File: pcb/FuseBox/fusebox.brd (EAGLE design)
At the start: 160 x 100 mm, 102 parts, among them Q1 IRF510PbF, U1 ESP32-DEVKITC-32D, U2 TEXAS_INSTRUMENTS_TPS563249DD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, U3 MAXIM_ELECTRONICS_MAX7221CWGM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, U4 TEXAS_INSTRUMENTS_ADS1015IDGS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, U5 TEXAS_INSTRUMENTS_PCF8574PWTE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, U6 TEXAS_INSTRUMENTS_PCF8574PWTE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

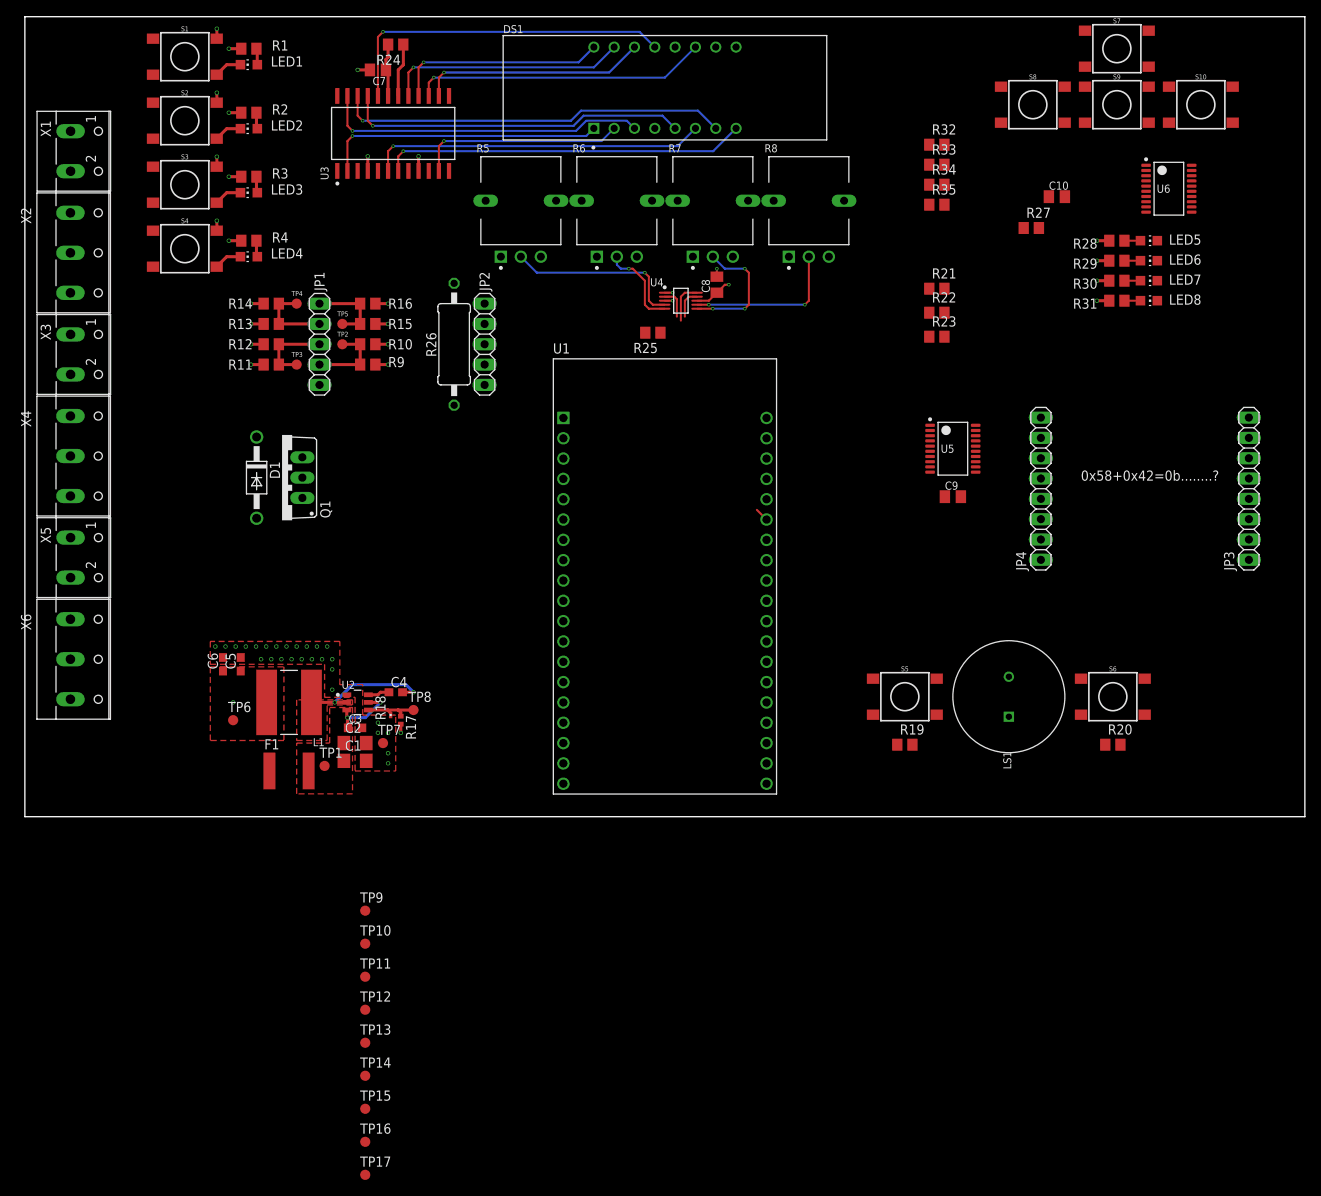
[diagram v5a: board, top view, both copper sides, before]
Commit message: Further work on PCB, almost done. Just have to route I2C and SPI lanes.
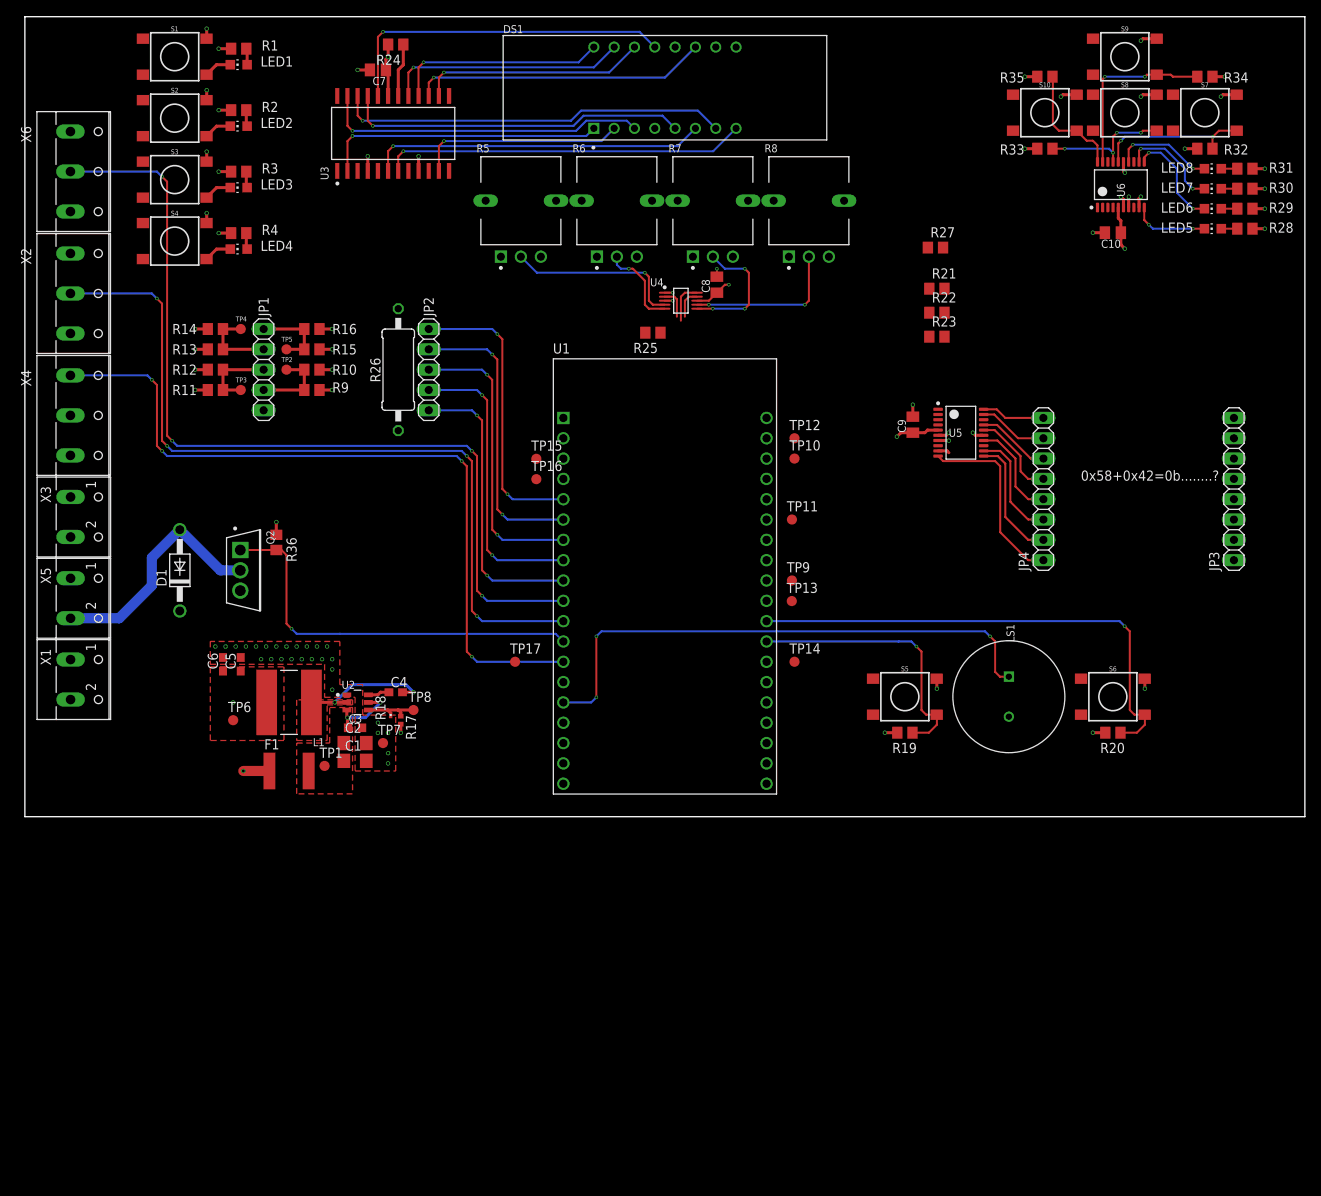
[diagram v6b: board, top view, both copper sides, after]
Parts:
- removed Q1: IRF510PbF, transistor-power:TO220BV
- added Q2: INFINEON_IRLB8721PBFINFINEON_IRLB8721PBF_0_0, Infineon - IRLB8721PbF:INFINEON_IRLB8721PBF_0
- added R36: 10k, rcl:R0805
- moved TP12 89.3 mm to (96.2, 47.3)
- moved TP16 85.6 mm to (63.9, 42.2)
- moved TP15 84.0 mm to (63.9, 44.7)
- moved TP10 81.0 mm to (96.2, 44.8)
- moved TP11 78.2 mm to (95.9, 37.1)
- moved TP13 76.8 mm to (95.9, 27.0)
- moved TP14 74.5 mm to (96.2, 19.4)
- moved TP9 67.4 mm to (95.9, 29.5)
- moved TP17 66.8 mm to (61.3, 19.4)
- moved X1 66.0 mm to (6.99, 17.1)
- moved X6 61.0 mm to (6.99, 80.6)
- moved R34 36.1 mm to (147.5, 92.5), turned to 180 degrees
- moved R32 33.5 mm to (147.5, 83.5)
- moved R31 23.0 mm to (152.5, 81.0), turned to 0 degrees
- moved R35 20.9 mm to (127.5, 92.5)
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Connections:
- net GND: now also Q2.3, R36.1; no longer Q1.S
- net LOCK_0: now also Q2.1, R36.2; no longer Q1.G
- net N$25: now also Q2.2; no longer Q1.D
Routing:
- net +5V: track 50.5 -> 212.6 mm, vias 2 -> 3
- net LASER_SENSE: track 0.00 -> 112.3 mm, vias 0 -> 4
- net LED_RING: track 0.00 -> 99.6 mm, vias 0 -> 4
- net CS_MAX7219_LEDM: track 0.00 -> 94.5 mm, vias 0 -> 4
- net PIEZO_0: track 0.00 -> 68.4 mm, vias 0 -> 3
- net BUTTON_1: track 0.00 -> 62.6 mm, vias 0 -> 1
- net +12V: track 0.00 -> 54.5 mm, vias 0 -> 1
- net LOCK_0: track 0.00 -> 50.1 mm, vias 0 -> 1
- net REWIRE_0_4: track 0.00 -> 36.6 mm, vias 0 -> 2
- net REWIRE_0_3: track 0.00 -> 36.6 mm, vias 0 -> 2
- net REWIRE_0_2: track 0.00 -> 36.6 mm, vias 0 -> 2
- net REWIRE_0_1: track 0.00 -> 36.6 mm, vias 0 -> 2
- net REWIRE_0_0: track 0.00 -> 36.6 mm, vias 0 -> 2
- net BUTTON_0: track 0.00 -> 34.1 mm, vias 0 -> 1
- net N$25: track 0.00 -> 29.9 mm
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
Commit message: Finished 1st version of layout
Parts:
- moved R27 46.7 mm to (73.7, 47.3), turned to 90 degrees
- moved R23 45.2 mm to (73.7, 39.7), turned to 270 degrees
- moved R21 31.7 mm to (86.4, 50.5)
- moved R22 29.4 mm to (86.4, 53.0)
- moved R25 9.28 mm to (86.4, 55.6), turned to 0 degrees
- moved TP17 2.54 mm to (63.8, 19.4)
- moved LED4 1.76 mm to (26.7, 72.7)
- moved S4 1.71 mm to (18.7, 73.7)
- moved R4 1.66 mm to (26.7, 74.6)
- moved LED3 1.06 mm to (26.7, 79.7)
- moved S3 1.01 mm to (18.7, 80.6)
- moved R3 0.96 mm to (26.7, 81.6)
- moved R1 0.44 mm to (26.7, 95.6)
- moved S1 0.39 mm to (18.7, 94.6)
- moved LED2 0.36 mm to (26.7, 86.7)
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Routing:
- net SPI_CLK: track 0.00 -> 180.4 mm, vias 0 -> 7
- net SPI_MOSI: track 0.00 -> 162.2 mm, vias 0 -> 7
- net SDA: track 3.73 -> 124.3 mm, vias 0 -> 4
- net SCL: track 5.23 -> 117.7 mm, vias 0 -> 6
- net PCF_INT_1: track 0.00 -> 101.5 mm, vias 0 -> 4
- net CS_MAX7221_7SEG: track 0.00 -> 96.0 mm, vias 0 -> 3
- net PCF_INT_0: track 0.00 -> 79.7 mm, vias 0 -> 4
- net ADC_RDY: track 3.84 -> 65.5 mm, vias 0 -> 3
- net +3V3: track 46.9 -> 55.0 mm, vias 22 -> 27
- net CS_MAX7219_LEDM: track 94.5 -> 99.5 mm
- net LED_RING: track 99.6 -> 101.1 mm
- net LASER_SENSE: track 112.3 -> 113.8 mm
- net REWIRE_0_1: track 36.6 -> 37.4 mm
- net REWIRE_0_4: track 36.6 -> 37.4 mm
- net REWIRE_0_2: track 36.6 -> 37.4 mm
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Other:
- board text added: "+12V"
- board text added: "+3V3"
- board text added: "+5V"
- board text added: "Drain"
- board text added: "GND"
- board text added: "LASER SENSE"
- board text added: "LED RING"
- board text added: "SPI CLK"
- board text added: "SPI MOSI"
- board text added: "Technische Fakultät, est. .... ?"
